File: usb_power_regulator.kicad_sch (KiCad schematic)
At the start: 10 parts, among them J1 USB_C_Receptacle_USB2.0_14P, U2 XC6206P302

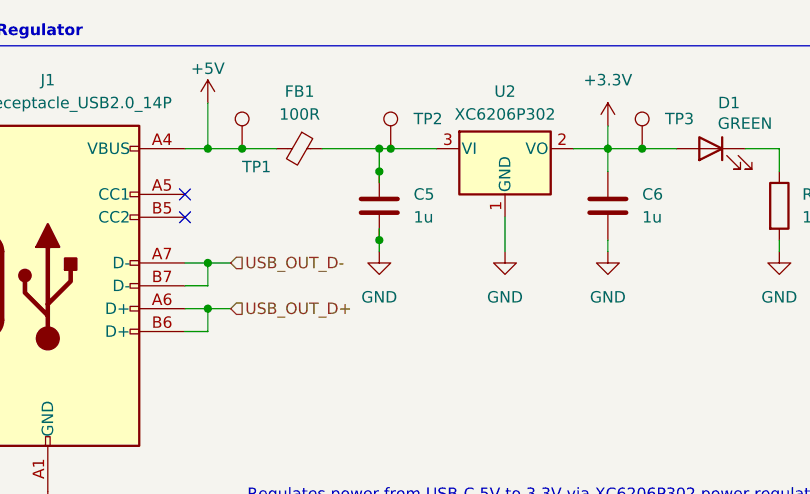
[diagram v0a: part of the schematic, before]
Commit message: [feat] Add CAN transceiver SN65VHD230
Also ran ERC checks and add some exclusion ERC for the FT230XS due to
3V3OUT being an input pin rather than output pin
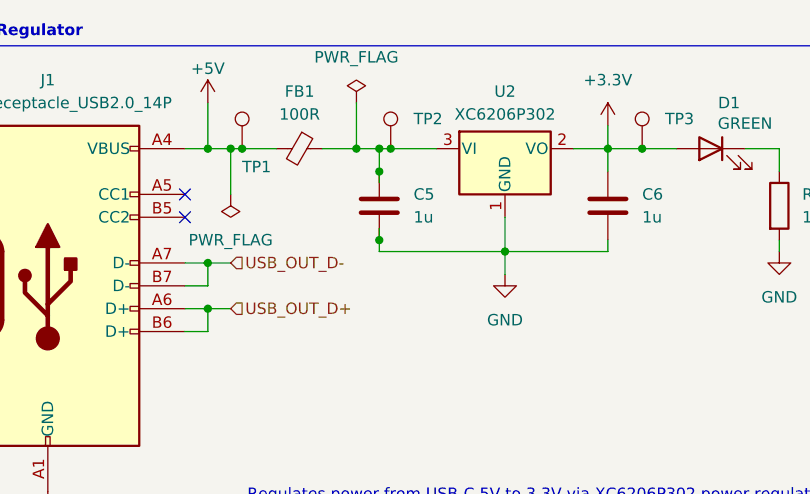
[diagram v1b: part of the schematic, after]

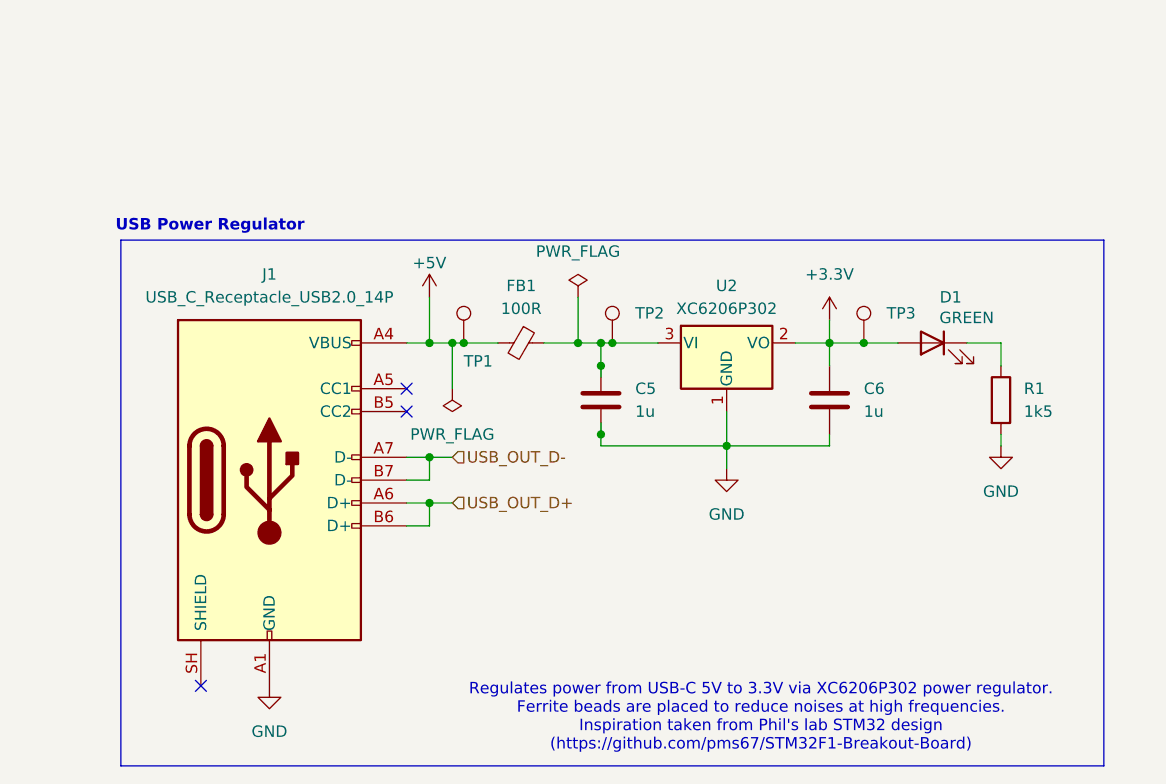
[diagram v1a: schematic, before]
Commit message: [feat] Add breakout for SPI1 for IMU
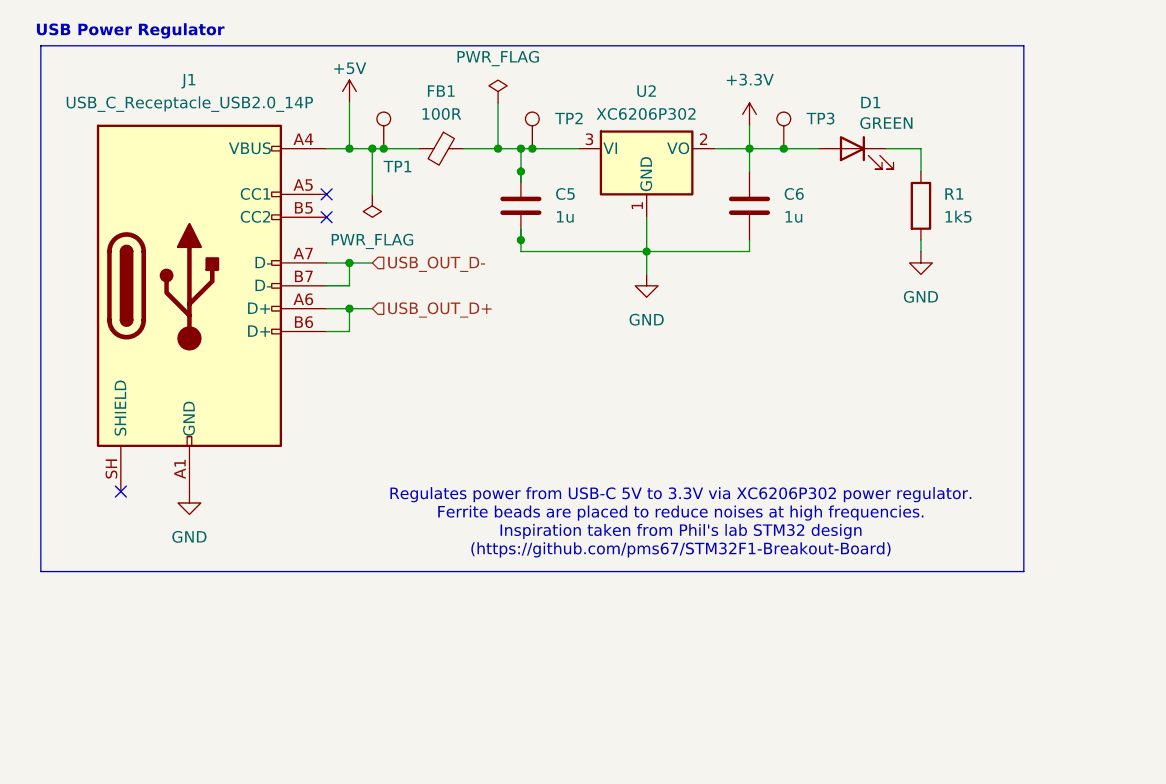
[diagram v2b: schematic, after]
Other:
- moved on the sheet: C5, C6, D1, FB1, J1, R1, TP1, TP2, TP3, U2

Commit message: [feat] Integrate MicroSD Card into the board with SPI2
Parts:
- J1: footprint (none) -> Connector_USB:USB_C_Receptacle_GCT_USB4105-xx-A_16P_TopMnt_Horizontal
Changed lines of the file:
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@@
 			)
 		)
-		(property "Footprint" ""
+		(property "Footprint" "Connector_USB:USB_C_Receptacle_GCT_USB4105-xx-A_16P_TopMnt_Horizontal"
 			(at 107.95 95.25 0)
 			(hide yes)
@@
 			)
 		)
-		(property "Datasheet" "https://www.usb.org/sites/default/files/documents/usb_type-c.zip"
+		(property "Datasheet" "https://www.mouser.com/catalog/specsheets/Global_Connector_Technology_usb4105.pdf"
 			(at 107.95 95.25 0)
 			(hide yes)

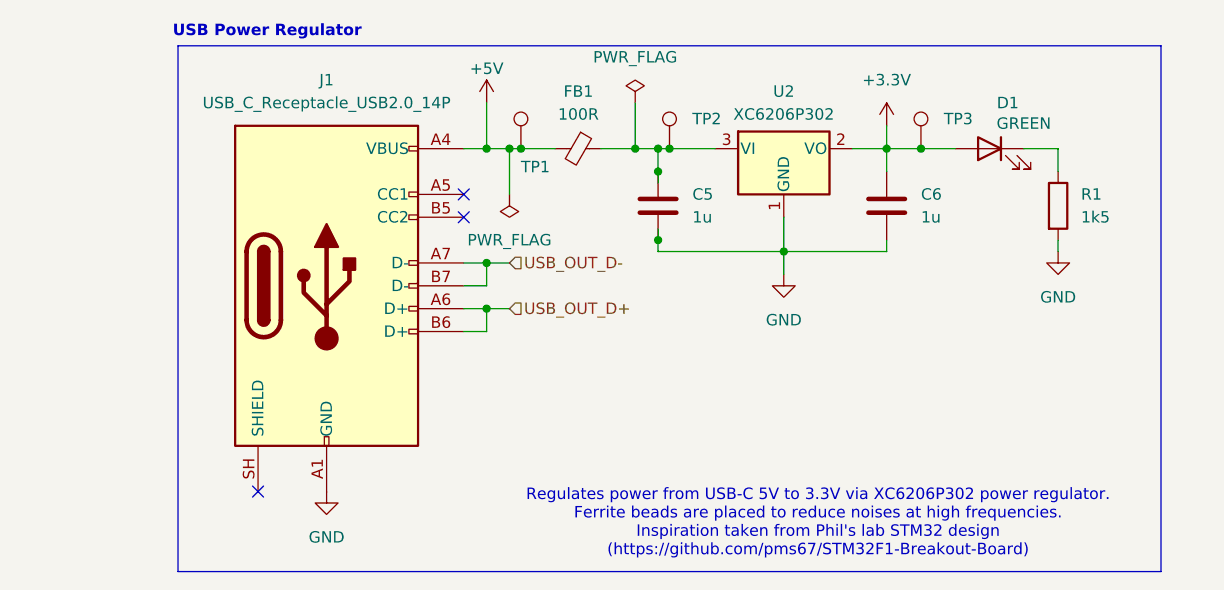
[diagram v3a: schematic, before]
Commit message: [fix] Add 5.1kR to CC1 and CC2 USB
USB-C specification requires CC1 and CC2 to be connected to ground via a
resistor for USB-C to USB-C power to work.
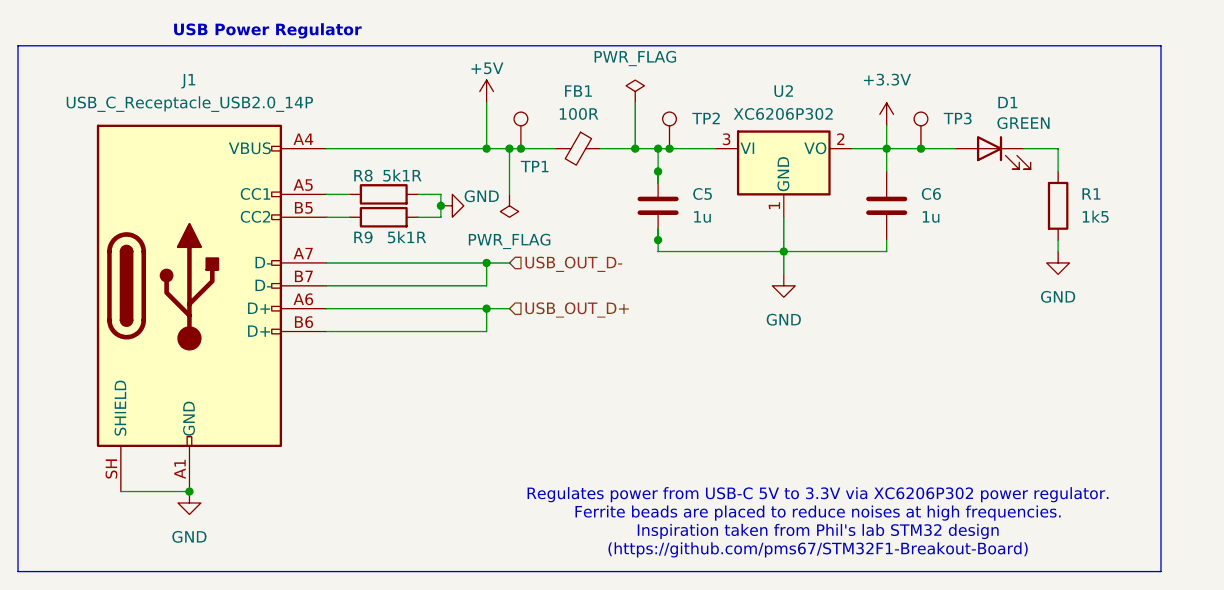
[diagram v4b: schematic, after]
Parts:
- added R8, R9: 5k1R, Resistor_SMD:R_0603_1608Metric, symbol Device:R
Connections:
- net GND: now also J1.SH (SHIELD), R8.2, R9.2
- net at J1.A5 (CC1): now also R8.1
- net at J1.B5 (CC2): now also R9.1
- no-connect marks 3 -> 0
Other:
- moved on the sheet: J1

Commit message: [feat] Add I2C breakout
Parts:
- J1: value USB_C_Receptacle_USB2.0_14P -> USB_C_Receptacle_USB2.0_16P; symbol Connector:USB_C_Receptacle_USB2.0_14P -> Connector:USB_C_Receptacle_USB2.0_16P
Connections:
- no-connect marks 0 -> 2
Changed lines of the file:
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@@
 		(color 0 0 0 0)
+	)
+	(no_connect
+		(at 104.14 110.49)
+	)
+	(no_connect
+		(at 104.14 107.95)
 	)
 	(wire
@@
 	)
 	(symbol
-		(lib_id "Connector:USB_C_Receptacle_USB2.0_14P")
+		(lib_id "Connector:USB_C_Receptacle_USB2.0_16P")
 		(at 88.9 95.25 0)
 		(unit 1)
@@
 			)
 		)
-		(property "Value" "USB_C_Receptacle_USB2.0_14P"
+		(property "Value" "USB_C_Receptacle_USB2.0_16P"
 			(at 88.9 74.93 0)
 			(show_name no)
@@
 			)
 		)
-		(property "Datasheet" "https://www.mouser.com/catalog/specsheets/Global_Connector_Technology_usb4105.pdf"
+		(property "Datasheet" "https://www.usb.org/sites/default/files/documents/usb_type-c.zip"
 			(at 92.71 95.25 0)
 			(hide yes)
@@
 			)
 		)
-		(property "Description" "USB 2.0-only 14P Type-C Receptacle connector"
+		(property "Description" "USB 2.0-only 16P Type-C Receptacle connector"
 			(at 88.9 95.25 0)
 			(hide yes)
@@
 		(pin "A1"
 		)
+		(pin "A8"
+		)
+		(pin "B8"
+		)
 		(instances

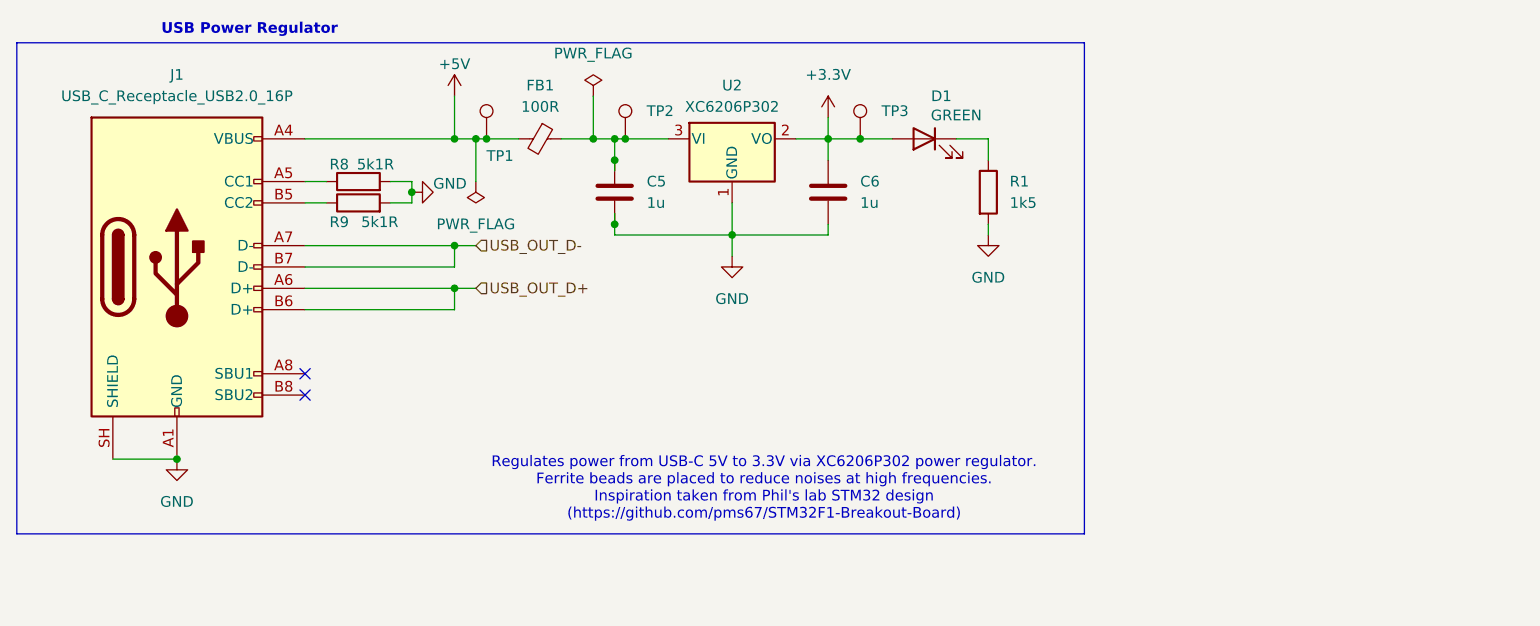
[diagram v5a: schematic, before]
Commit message: [feat] Add OLED I2C breakout for display, Add general purpose GPIOs
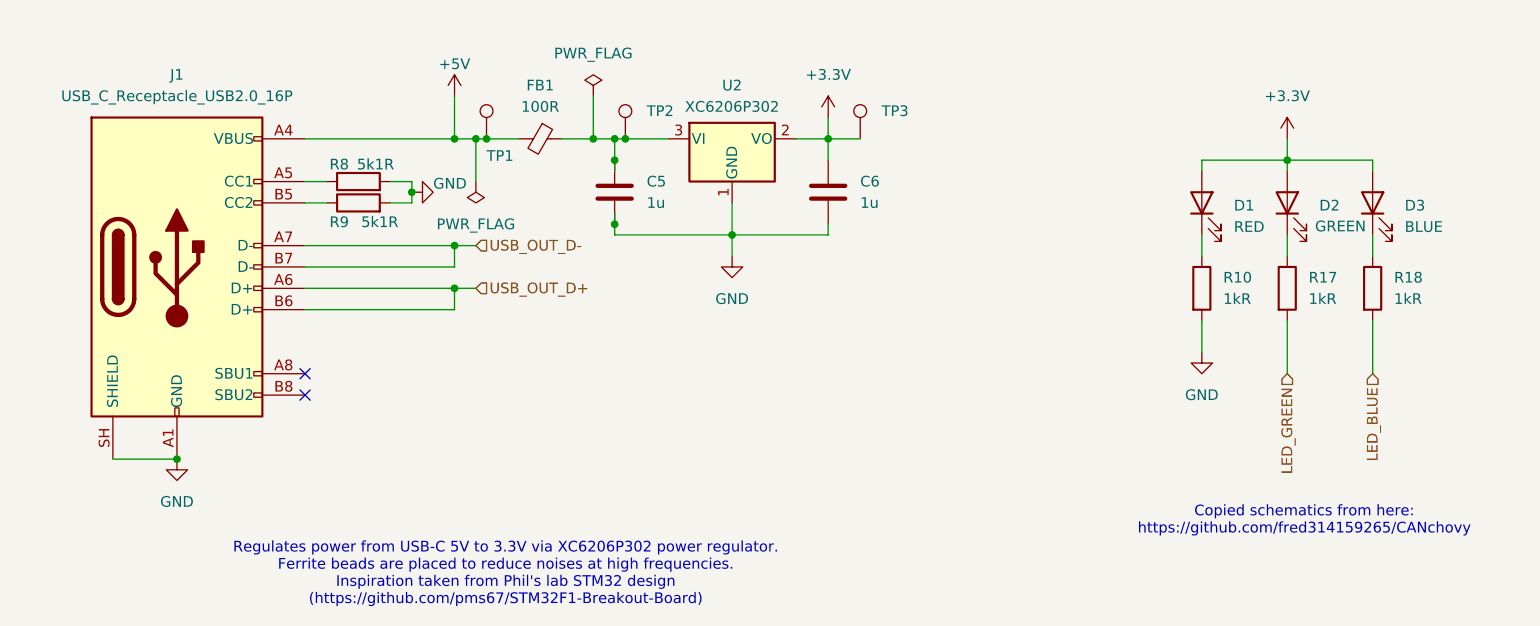
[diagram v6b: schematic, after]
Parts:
- removed R1: 1k5, Resistor_SMD:R_0603_1608Metric, symbol Device:R
- added D2: GREEN, symbol Device:LED
- added D3: BLUE, symbol Device:LED
- added R10, R17, R18: 1kR, Resistor_SMD:R_0603_1608Metric, symbol Device:R
- D1: value GREEN -> RED; footprint LED_SMD:LED_0603_1608Metric -> (none)
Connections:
- net +3.3V: now also D2.2 (A), D3.2 (A)
- net GND: now also R10.2
- net at D1.1 (K): now also R10.1
- new net: D3.1 (K), R18.1
- new net: D2.1 (K), R17.1
- new net LED_BLUE: R18.2
- new net LED_GREEN: R17.2
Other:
- note added: "Copied schematics from here: https://github.com/fred314159265/CANchovy"
- note removed: "USB Power Regulator"

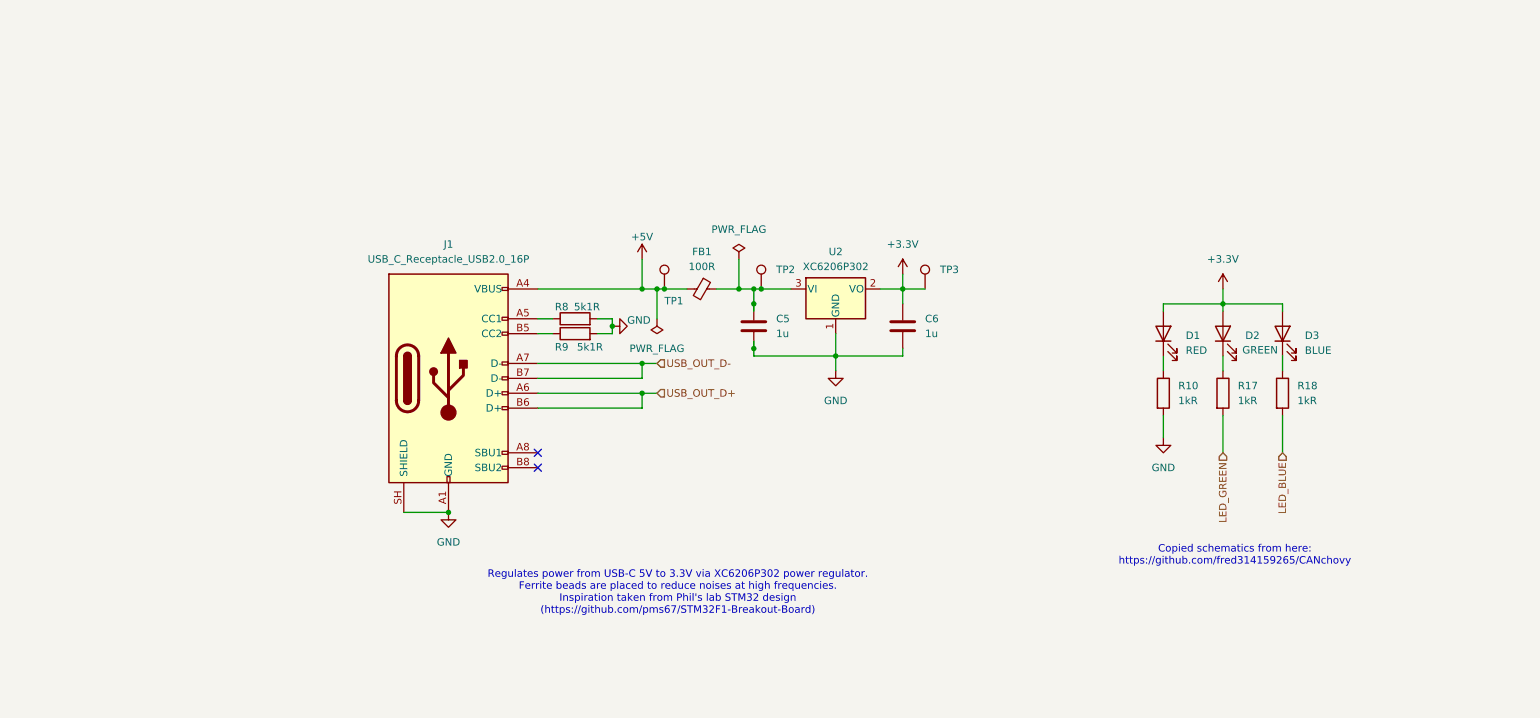
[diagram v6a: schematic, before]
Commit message: [feat] Integrate external battery
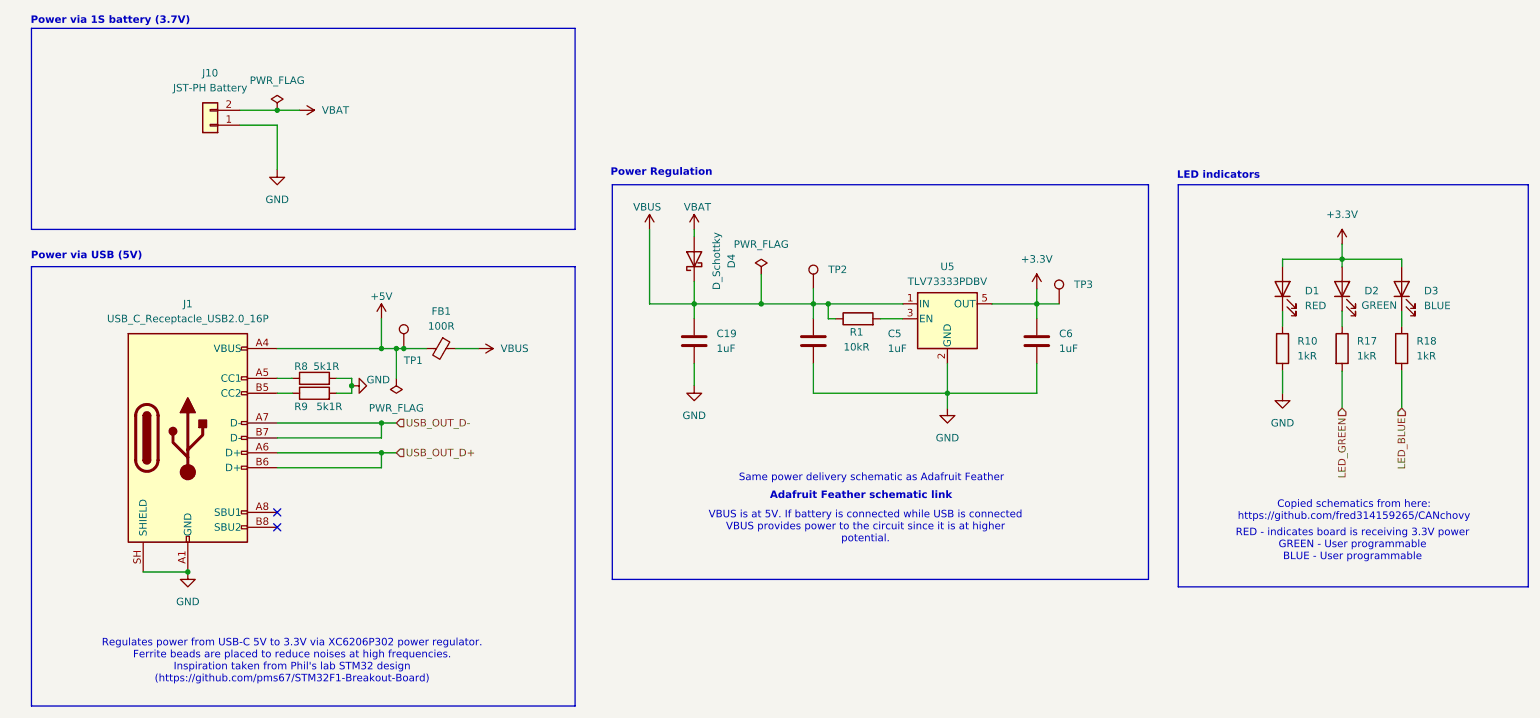
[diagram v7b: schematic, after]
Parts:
- removed U2: XC6206P302, Package_TO_SOT_SMD:SOT-23-3, symbol Regulator_Linear:XC6206PxxxMR
- added C19: 1uF, Capacitor_SMD:C_0603_1608Metric, symbol Device:C
- added D4: D_Schottky, Diode_SMD:D_0603_1608Metric, symbol Device:D_Schottky
- added J10: JST-PH Battery, Connector_JST:JST_PH_S2B-PH-K_1x02_P2.00mm_Horizontal, symbol Connector_Generic:Conn_01x02
- added R1: 10kR, Resistor_SMD:R_0603_1608Metric, symbol Device:R
- added U5: TLV73333PDBV, Package_TO_SOT_SMD:SOT-23-5, symbol Regulator_Linear:TLV73333PDBV
- C5, C6: value 1u -> 1uF
- D1, D2, D3: footprint (none) -> LED_SMD:LED_0603_1608Metric
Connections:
- net +3.3V: now also U5.5 (OUT)
- net GND: now also C19.2, J10.1 (Pin_1), U5.2 (GND)
- net VBUS: now reaches C5.1, FB1.1, TP2.1
- net VBUS: now also C19.1, D4.1 (K), R1.1, U5.1 (IN)
- new net: R1.2, U5.3 (EN)
- new net VBAT: D4.2 (A), J10.2 (Pin_2)
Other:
- note added: "Adafruit Feather schematic link"
- note added: "LED indicators"
- note added: "Power Regulation"
- note added: "Power via 1S battery (3.7V)"
- note added: "Power via USB (5V)"
- note added: "RED - indicates board is receiving 3.3V power GREEN - User programmable BLUE - User programmable"
- note added: "Same power delivery schematic as Adafruit Feather"
- note added: "VBUS is at 5V. If battery is connected while USB is connected VBUS provides power to the circuit since it is at higher potential."
- moved on the sheet: C5, C6, D1, D2, D3, R10, R17, R18, TP2, TP3
